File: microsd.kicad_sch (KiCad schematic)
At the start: 8 parts, among them J7 503398-1892

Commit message: bozza layout pcb
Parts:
- RN6, RN7, RN8, RN9: footprint resistor_pack_0603x4:resistor_array_0603x4 -> Resistor_SMD:R_Array_Convex_4x0603
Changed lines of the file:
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@@
+	(wire
+		(pts
+			(xy 153.67 35.56) (xy 157.48 35.56)
+		)
+		(stroke
+			(width 0)
+			(type default)
+		)
+	)
 	(wire
 		(pts
@@
 	)
 	(symbol
+		(lib_id "power:+3V3")
+		(at 153.67 35.56 90)
+		(unit 1)
+		(exclude_from_sim no)
+		(in_bom yes)
+		(on_board yes)
+		(dnp no)
+		(fields_autoplaced yes)
+		(property "Reference" "#PWR088"
+			(at 157.48 35.56 0)
+			(effects
+				(font
+					(size 1.27 1.27)
+				)
+				(hide yes)
+			)
+		)
+		(property "Value" "+3V3"
+			(at 149.86 35.5599 90)
+			(effects
+				(font
+					(size 1.27 1.27)
+				)
+				(justify left)
+			)
+		)
+		(property "Footprint" ""
+			(at 153.67 35.56 0)
+			(effects
+				(font
+					(size 1.27 1.27)
+				)
+				(hide yes)
+			)
+		)
+		(property "Datasheet" ""
+			(at 153.67 35.56 0)
+			(effects
+				(font
+					(size 1.27 1.27)
+				)
+				(hide yes)
+			)
+		)
+		(property "Description" "Power symbol creates a global label with name \"+3V3\""
+			(at 153.67 35.56 0)
+			(effects
+				(font
+					(size 1.27 1.27)
+				)
+				(hide yes)
+			)
+		)
+		(pin "1"
+		)
+		(instances
+			(project ""
+				(path "/105f6e80-8e20-4d56-8eb3-6fa826818670/5f928ec3-de2c-45ad-87ae-24994ae19594"
+					(reference "#PWR088")
+					(unit 1)
+				)
+			)
+		)
+	)
+	(symbol
 		(lib_id "Device:C_Small")
 		(at 52.07 67.31 0)
@@
 			)
 		)
-		(property "Footprint" "resistor_pack_0603x4:resistor_array_0603x4"
+		(property "Footprint" "Resistor_SMD:R_Array_Convex_4x0603"
 			(at 166.37 75.565 90)
 			(effects
@@
 			)
 		)
-		(property "Footprint" "resistor_pack_0603x4:resistor_array_0603x4"
+		(property "Footprint" "Resistor_SMD:R_Array_Convex_4x0603"
 			(at 81.915 34.29 90)
 			(effects
@@
 			)
 		)
-		(property "Footprint" "resistor_pack_0603x4:resistor_array_0603x4"
+		(property "Footprint" "Resistor_SMD:R_Array_Convex_4x0603"
 			(at 137.795 80.01 90)
 			(effects
@@
 	)
 	(symbol
+		(lib_id "power:+3.3V")
+		(at 157.48 35.56 270)
+		(unit 1)
+		(exclude_from_sim no)
+		(in_bom yes)
+		(on_board yes)
+		(dnp no)
+		(fields_autoplaced yes)
+		(property "Reference" "#PWR087"
+			(at 153.67 35.56 0)
+			(effects
+				(font
+					(size 1.27 1.27)
+				)
+				(hide yes)
+			)
+		)
+		(property "Value" "+3.3V"
+			(at 161.29 35.5599 90)
+			(effects
+				(font
+					(size 1.27 1.27)
+				)
+				(justify left)
+			)
+		)
+		(property "Footprint" ""
+			(at 157.48 35.56 0)
+			(effects
+				(font
+					(size 1.27 1.27)
+				)
+				(hide yes)
+			)
+		)
+		(property "Datasheet" ""
+			(at 157.48 35.56 0)
+			(effects
+				(font
+					(size 1.27 1.27)
+				)
+				(hide yes)
+			)
+		)
+		(property "Description" "Power symbol creates a global label with name \"+3.3V\""
+			(at 157.48 35.56 0)
+			(effects
+				(font
+					(size 1.27 1.27)
+				)
+				(hide yes)
+			)
+		)
+		(pin "1"
+		)
+		(instances
+			(project "TABv1"
+				(path "/105f6e80-8e20-4d56-8eb3-6fa826818670/5f928ec3-de2c-45ad-87ae-24994ae19594"
+					(reference "#PWR087")
+					(unit 1)
+				)
+			)
+		)
+	)
+	(symbol
 		(lib_id "Device:R_Pack04")
 		(at 45.72 48.26 90)
@@
 			)
 		)
-		(property "Footprint" "resistor_pack_0603x4:resistor_array_0603x4"
+		(property "Footprint" "Resistor_SMD:R_Array_Convex_4x0603"
 			(at 45.72 41.275 90)
 			(effects

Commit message: Corrections
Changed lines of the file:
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@@
-	(wire
-		(pts
-			(xy 153.67 35.56) (xy 157.48 35.56)
-		)
-		(stroke
-			(width 0)
-			(type default)
-		)
-	)
 	(wire
 		(pts
@@
 	)
 	(symbol
-		(lib_id "power:+3V3")
-		(at 153.67 35.56 90)
-		(unit 1)
-		(exclude_from_sim no)
-		(in_bom yes)
-		(on_board yes)
-		(dnp no)
-		(fields_autoplaced yes)
-		(property "Reference" "#PWR088"
-			(at 157.48 35.56 0)
-			(effects
-				(font
-					(size 1.27 1.27)
-				)
-				(hide yes)
-			)
-		)
-		(property "Value" "+3V3"
-			(at 149.86 35.5599 90)
-			(effects
-				(font
-					(size 1.27 1.27)
-				)
-				(justify left)
-			)
-		)
-		(property "Footprint" ""
-			(at 153.67 35.56 0)
-			(effects
-				(font
-					(size 1.27 1.27)
-				)
-				(hide yes)
-			)
-		)
-		(property "Datasheet" ""
-			(at 153.67 35.56 0)
-			(effects
-				(font
-					(size 1.27 1.27)
-				)
-				(hide yes)
-			)
-		)
-		(property "Description" "Power symbol creates a global label with name \"+3V3\""
-			(at 153.67 35.56 0)
-			(effects
-				(font
-					(size 1.27 1.27)
-				)
-				(hide yes)
-			)
-		)
-		(pin "1"
-		)
-		(instances
-			(project ""
-				(path "/105f6e80-8e20-4d56-8eb3-6fa826818670/5f928ec3-de2c-45ad-87ae-24994ae19594"
-					(reference "#PWR088")
-					(unit 1)
-				)
-			)
-		)
-	)
-	(symbol
 		(lib_id "Device:C_Small")
 		(at 52.07 67.31 0)
@@
 					(unit 1)
 				)
-			)
-		)
-	)
-	(symbol
-		(lib_id "power:+3.3V")
-		(at 157.48 35.56 270)
-		(unit 1)
-		(exclude_from_sim no)
-		(in_bom yes)
-		(on_board yes)
-		(dnp no)
-		(fields_autoplaced yes)
-		(property "Reference" "#PWR087"
-			(at 153.67 35.56 0)
-			(effects
-				(font
-					(size 1.27 1.27)
-				)
-				(hide yes)
-			)
-		)
-		(property "Value" "+3.3V"
-			(at 161.29 35.5599 90)
-			(effects
-				(font
-					(size 1.27 1.27)
-				)
-				(justify left)
-			)
-		)
-		(property "Footprint" ""
-			(at 157.48 35.56 0)
-			(effects
-				(font
-					(size 1.27 1.27)
-				)
-				(hide yes)
-			)
-		)
-		(property "Datasheet" ""
-			(at 157.48 35.56 0)
-			(effects
-				(font
-					(size 1.27 1.27)
-				)
-				(hide yes)
-			)
-		)
-		(property "Description" "Power symbol creates a global label with name \"+3.3V\""
-			(at 157.48 35.56 0)
-			(effects
-				(font
-					(size 1.27 1.27)
-				)
-				(hide yes)
-			)
-		)
-		(pin "1"
-		)
-		(instances
-			(project "TABv1"
-				(path "/105f6e80-8e20-4d56-8eb3-6fa826818670/5f928ec3-de2c-45ad-87ae-24994ae19594"
-					(reference "#PWR087")
-					(unit 1)
-				)

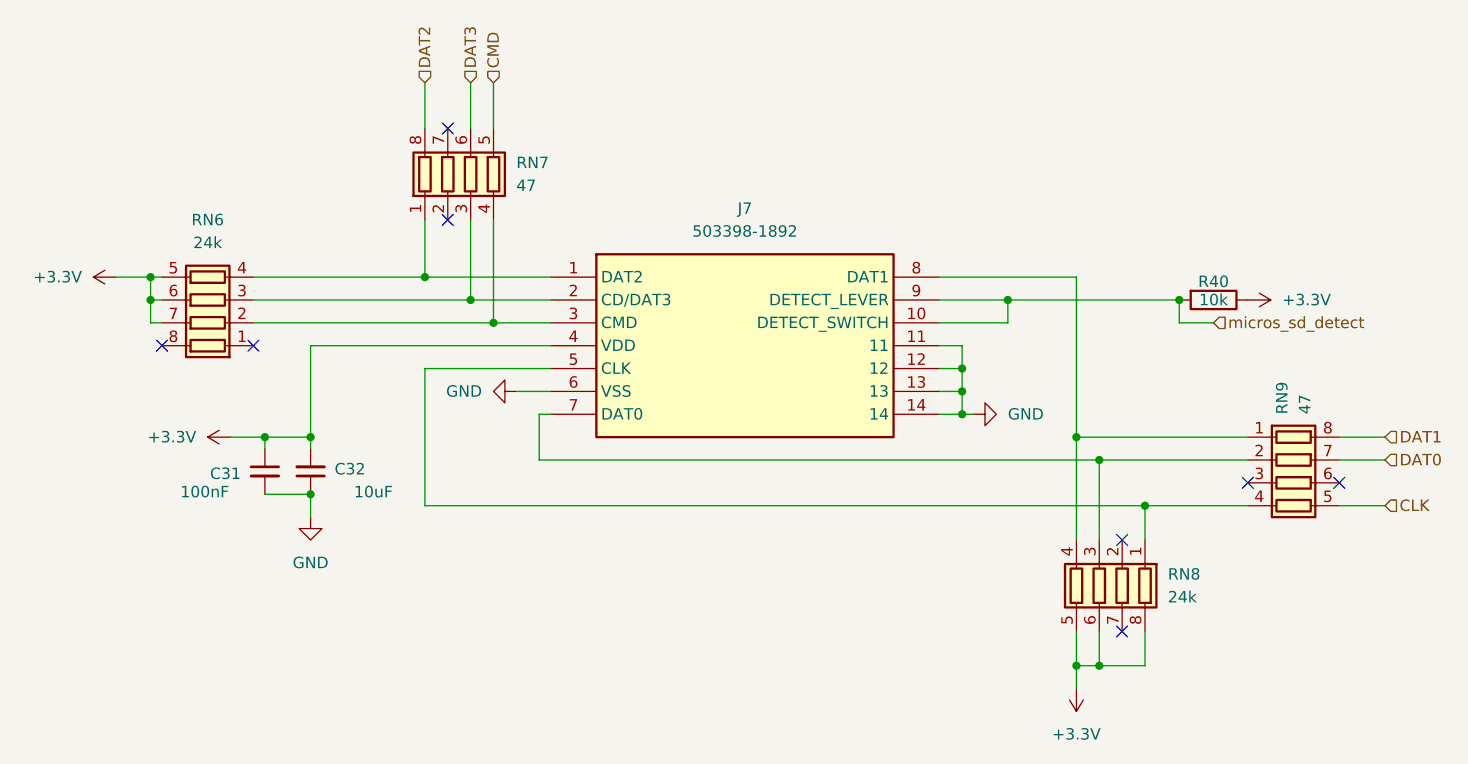
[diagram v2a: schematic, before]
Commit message: NET allignment (all on +3V3)
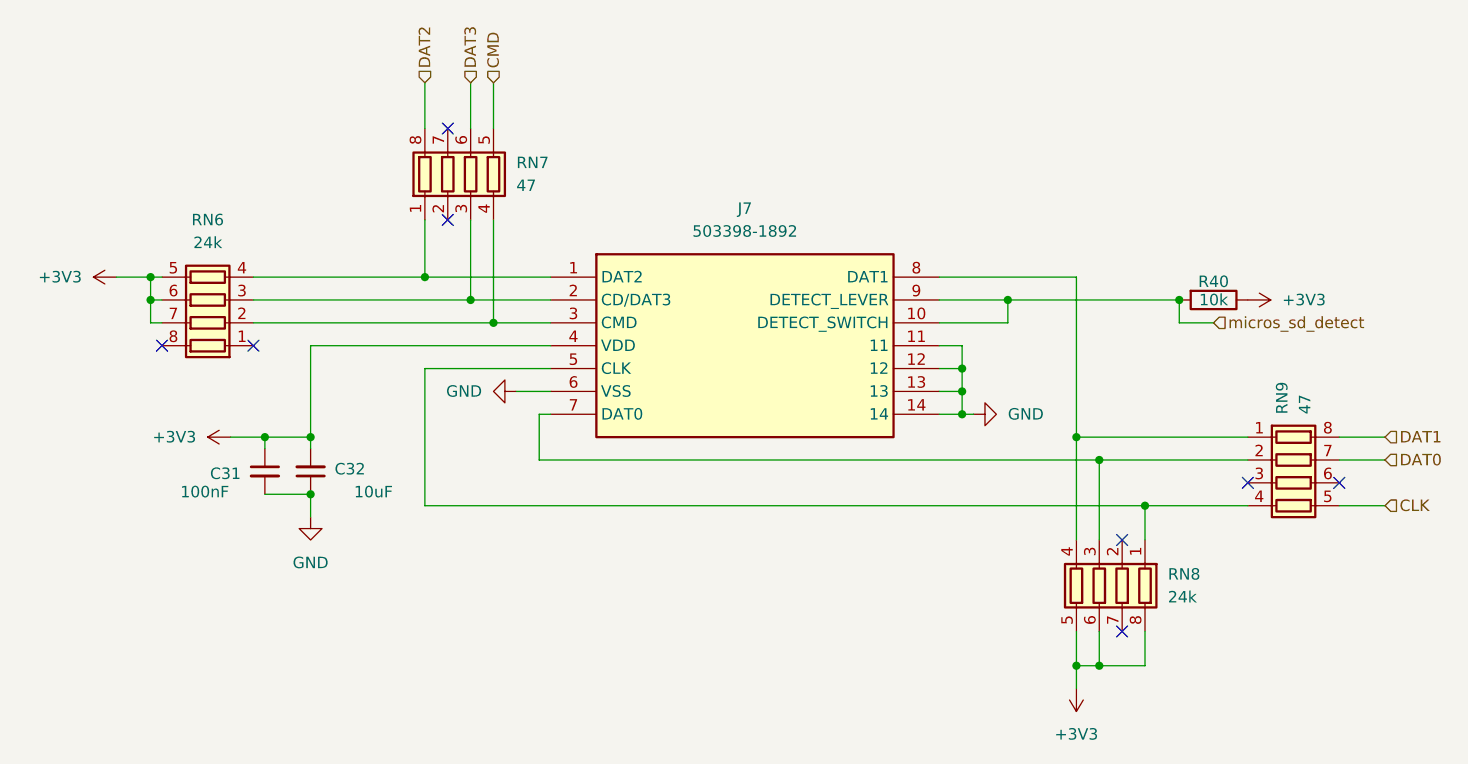
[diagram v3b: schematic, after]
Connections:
- net +3.3V renamed +3V3
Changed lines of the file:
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@@
 			)
 		)
-		(property "Value" "+3.3V"
+		(property "Value" "+3V3"
 			(at 44.45 63.4999 90)
 			(effects
@@
 			)
 		)
-		(property "Description" "Power symbol creates a global label with name \"+3.3V\""
+		(property "Description" "Power symbol creates a global label with name \"+3V3\""
 			(at 48.26 63.5 0)
 			(effects
@@
 			)
 		)
-		(property "Value" "+3.3V"
+		(property "Value" "+3V3"
 			(at 142.24 96.52 0)
 			(effects
@@
 			)
 		)
-		(property "Description" "Power symbol creates a global label with name \"+3.3V\""
+		(property "Description" "Power symbol creates a global label with name \"+3V3\""
 			(at 142.24 91.44 0)
 			(effects
@@
 			)
 		)
-		(property "Value" "+3.3V"
+		(property "Value" "+3V3"
 			(at 31.75 45.7199 90)
 			(effects
@@
 			)
 		)
-		(property "Description" "Power symbol creates a global label with name \"+3.3V\""
+		(property "Description" "Power symbol creates a global label with name \"+3V3\""
 			(at 35.56 45.72 0)
 			(effects
@@
 			)
 		)
-		(property "Value" "+3.3V"
+		(property "Value" "+3V3"
 			(at 165.1 48.2599 90)
 			(effects
@@
 			)
 		)
-		(property "Description" "Power symbol creates a global label with name \"+3.3V\""
+		(property "Description" "Power symbol creates a global label with name \"+3V3\""
 			(at 161.29 48.26 0)
 			(effects

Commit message: ROUTING
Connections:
- net CLK: now also RN9.7 (R2.2); no longer RN9.5 (R4.2)
- net DAT0: now also RN9.5 (R4.2); no longer RN9.7 (R2.2)
- net DAT2: now also J7.1 (DAT2), RN6.4 (R4.1), RN7.1 (R1.1)
- net DAT3: now also J7.2 (CD/DAT3), RN6.3 (R3.1), RN7.3 (R3.1)
- net _DAT1: now reaches J7.8 (DAT1), RN9.1 (R1.1)
- net _DAT1: now also RN8.1 (R1.1); no longer RN8.4 (R4.1)
- net at J7.7 (DAT0), RN8.3 (R3.1): now also RN9.4 (R4.1); no longer RN9.2 (R2.1)
- new net: J7.5 (CLK), RN8.4 (R4.1), RN9.2 (R2.1)
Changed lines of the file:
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@@
-	)
-	(junction
-		(at 142.24 63.5)
-		(diameter 0)
-		(color 0 0 0 0)
 	)
 	(junction
@@
 	)
 	(junction
+		(at 142.24 66.04)
+		(diameter 0)
+		(color 0 0 0 0)
+	)
+	(junction
 		(at 144.78 88.9)
 		(diameter 0)
@@
 	)
 	(junction
+		(at 144.78 71.12)
+		(diameter 0)
+		(color 0 0 0 0)
+	)
+	(junction
 		(at 129.54 60.96)
 		(diameter 0)
@@
 	)
 	(junction
-		(at 144.78 66.04)
-		(diameter 0)
-		(color 0 0 0 0)
-	)
-	(junction
 		(at 129.54 55.88)
 		(diameter 0)
@@
 	)
 	(junction
-		(at 149.86 71.12)
-		(diameter 0)
-		(color 0 0 0 0)
-	)
-	(junction
 		(at 52.07 63.5)
 		(diameter 0)
@@
 	(junction
 		(at 39.37 45.72)
+		(diameter 0)
+		(color 0 0 0 0)
+	)
+	(junction
+		(at 149.86 63.5)
 		(diameter 0)
 		(color 0 0 0 0)
@@
 	(wire
 		(pts
+			(xy 142.24 66.04) (xy 142.24 74.93)
+		)
+		(stroke
+			(width 0)
+			(type default)
+		)
+	)
+	(wire
+		(pts
 			(xy 74.93 48.26) (xy 83.82 48.26)
 		)
@@
 	(wire
 		(pts
-			(xy 149.86 71.12) (xy 161.29 71.12)
-		)
-		(stroke
-			(width 0)
-			(type default)
-		)
-	)
-	(wire
-		(pts
 			(xy 77.47 24.13) (xy 77.47 29.21)
 		)
@@
 	(wire
 		(pts
-			(xy 142.24 63.5) (xy 142.24 74.93)
-		)
-		(stroke
-			(width 0)
-			(type default)
-		)
-	)
-	(wire
-		(pts
 			(xy 129.54 53.34) (xy 129.54 55.88)
 		)
@@
 	(wire
 		(pts
+			(xy 142.24 45.72) (xy 142.24 63.5)
+		)
+		(stroke
+			(width 0)
+			(type default)
+		)
+	)
+	(wire
+		(pts
 			(xy 134.62 48.26) (xy 153.67 48.26)
 		)
@@
 	(wire
 		(pts
-			(xy 82.55 66.04) (xy 144.78 66.04)
+			(xy 82.55 71.12) (xy 144.78 71.12)
 		)
 		(stroke
@@
 	(wire
 		(pts
-			(xy 142.24 63.5) (xy 161.29 63.5)
+			(xy 142.24 63.5) (xy 149.86 63.5)
 		)
 		(stroke
@@
 	(wire
 		(pts
-			(xy 144.78 66.04) (xy 161.29 66.04)
-		)
-		(stroke
-			(width 0)
-			(type default)
-		)
-	)
-	(wire
-		(pts
-			(xy 69.85 55.88) (xy 69.85 71.12)
+			(xy 142.24 66.04) (xy 161.29 66.04)
+		)
+		(stroke
+			(width 0)
+			(type default)
+		)
+	)
+	(wire
+		(pts
+			(xy 69.85 55.88) (xy 69.85 66.04)
 		)
 		(stroke
@@
 	(wire
 		(pts
-			(xy 142.24 45.72) (xy 142.24 63.5)
-		)
-		(stroke
-			(width 0)
-			(type default)
-		)
-	)
-	(wire
-		(pts
 			(xy 39.37 48.26) (xy 39.37 50.8)
 		)
@@
 	(wire
 		(pts
-			(xy 69.85 71.12) (xy 149.86 71.12)
+			(xy 69.85 66.04) (xy 142.24 66.04)
 		)
 		(stroke
@@
 	(wire
 		(pts
+			(xy 144.78 71.12) (xy 161.29 71.12)
+		)
+		(stroke
+			(width 0)
+			(type default)
+		)
+	)
+	(wire
+		(pts
 			(xy 127 55.88) (xy 129.54 55.88)
 		)
@@
 	(wire
 		(pts
-			(xy 82.55 60.96) (xy 82.55 66.04)
+			(xy 82.55 60.96) (xy 82.55 71.12)
 		)
 		(stroke
@@
 	(wire
 		(pts
-			(xy 144.78 66.04) (xy 144.78 74.93)
-		)
-		(stroke
-			(width 0)
-			(type default)
-		)
-	)
-	(wire
-		(pts
-			(xy 149.86 71.12) (xy 149.86 74.93)
+			(xy 149.86 63.5) (xy 149.86 74.93)
 		)
 		(stroke
@@
 	(wire
 		(pts
+			(xy 144.78 71.12) (xy 144.78 74.93)
+		)
+		(stroke
+			(width 0)
+			(type default)
+		)
+	)
+	(wire
+		(pts
 			(xy 74.93 39.37) (xy 74.93 48.26)
 		)
@@
 	(wire
 		(pts
+			(xy 149.86 63.5) (xy 161.29 63.5)
+		)
+		(stroke
+			(width 0)
+			(type default)
+		)
+	)
+	(wire
+		(pts
 			(xy 57.15 63.5) (xy 57.15 64.77)
 		)
@@
 		)
 	)
-	(hierarchical_label "DAT0"
+	(label "DAT3"
+		(at 78.74 48.26 0)
+		(effects
+			(font
+				(size 1.27 1.27)
+			)
+			(justify left bottom)
+		)
+	)
+	(label "DAT2"
+		(at 78.74 45.72 0)
+		(effects
+			(font
+				(size 1.27 1.27)
+			)
+			(justify left bottom)
+		)
+	)
+	(label "_DAT1"
+		(at 132.08 45.72 0)
+		(effects
+			(font
+				(size 1.27 1.27)
+			)
+			(justify left bottom)
+		)
+	)
+	(hierarchical_label "CLK"
 		(shape input)
 		(at 176.53 66.04 0)
@@
 		)
 	)
+	(hierarchical_label "DAT0"
+		(shape input)
+		(at 176.53 71.12 0)
+		(effects
+			(font
+				(size 1.27 1.27)
+			)
+			(justify left)
+		)
+	)
 	(hierarchical_label "DAT3"
 		(shape input)
@@
 		(effects
 			(font
-				(size 1.27 1.27)
-			)
-			(justify left)
-		)
-	)
-	(hierarchical_label "CLK"
-		(shape input)
-		(at 176.53 71.12 0)
-		(effects
-			(font

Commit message: Routing 06/25
Molte modifiche
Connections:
- net +3V3: now also RN6.8 (R1.2); no longer RN6.7 (R2.2)
- net CMD: now also RN7.6 (R3.2); no longer RN7.5 (R4.2)
- net DAT2: now also RN7.5 (R4.2); no longer J7.1 (DAT2), RN6.4 (R4.1), RN7.1 (R1.1), RN7.8 (R1.2)
- net DAT3: now also RN7.8 (R1.2); no longer J7.2 (CD/DAT3), RN6.3 (R3.1), RN7.3 (R3.1), RN7.6 (R3.2)
- net at RN6.1 (R1.1): now also J7.3 (CMD), RN7.3 (R3.1)
- new net _DAT2: J7.1 (DAT2), RN6.4 (R4.1), RN7.4 (R4.1)
- new net _DAT3: J7.2 (CD/DAT3), RN6.3 (R3.1), RN7.1 (R1.1)
- now unconnected: RN6.2 (R2.1)
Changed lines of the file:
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@@
-	)
-	(junction
-		(at 74.93 48.26)
-		(diameter 0)
-		(color 0 0 0 0)
 	)
 	(junction
@@
 	)
 	(junction
+		(at 74.93 50.8)
+		(diameter 0)
+		(color 0 0 0 0)
+	)
+	(junction
+		(at 144.78 71.12)
+		(diameter 0)
+		(color 0 0 0 0)
+	)
+	(junction
+		(at 129.54 60.96)
+		(diameter 0)
+		(color 0 0 0 0)
+	)
+	(junction
+		(at 129.54 55.88)
+		(diameter 0)
+		(color 0 0 0 0)
+	)
+	(junction
+		(at 69.85 48.26)
+		(diameter 0)
+		(color 0 0 0 0)
+	)
+	(junction
+		(at 57.15 69.85)
+		(diameter 0)
+		(color 0 0 0 0)
+	)
+	(junction
+		(at 52.07 63.5)
+		(diameter 0)
+		(color 0 0 0 0)
+	)
+	(junction
 		(at 39.37 48.26)
 		(diameter 0)
@@
 	)
 	(junction
-		(at 144.78 71.12)
-		(diameter 0)
-		(color 0 0 0 0)
-	)
-	(junction
-		(at 129.54 60.96)
-		(diameter 0)
-		(color 0 0 0 0)
-	)
-	(junction
-		(at 69.85 45.72)
-		(diameter 0)
-		(color 0 0 0 0)
-	)
-	(junction
-		(at 129.54 55.88)
-		(diameter 0)
-		(color 0 0 0 0)
-	)
-	(junction
-		(at 57.15 69.85)
-		(diameter 0)
-		(color 0 0 0 0)
-	)
-	(junction
-		(at 52.07 63.5)
-		(diameter 0)
-		(color 0 0 0 0)
-	)
-	(junction
 		(at 39.37 45.72)
 		(diameter 0)
@@
 	)
 	(junction
-		(at 77.47 50.8)
+		(at 77.47 45.72)
 		(diameter 0)
 		(color 0 0 0 0)
@@
 	)
 	(no_connect
+		(at 40.64 50.8)
+	)
+	(no_connect
 		(at 147.32 85.09)
-	)
-	(no_connect
-		(at 50.8 53.34)
 	)
 	(no_connect
@@
 	)
 	(no_connect
+		(at 50.8 50.8)
+	)
+	(no_connect
 		(at 171.45 68.58)
-	)
-	(no_connect
-		(at 40.64 53.34)
 	)
 	(no_connect
@@
 	(wire
 		(pts
-			(xy 74.93 48.26) (xy 83.82 48.26)
-		)
-		(stroke
-			(width 0)
-			(type default)
-		)
-	)
-	(wire
-		(pts
 			(xy 129.54 60.96) (xy 130.81 60.96)
 		)
@@
 	(wire
 		(pts
+			(xy 53.34 50.8) (xy 53.34 53.34)
+		)
+		(stroke
+			(width 0)
+			(type default)
+		)
+	)
+	(wire
+		(pts
 			(xy 52.07 63.5) (xy 57.15 63.5)
 		)
@@
 	(wire
 		(pts
+			(xy 69.85 48.26) (xy 83.82 48.26)
+		)
+		(stroke
+			(width 0)
+			(type default)
+		)
+	)
+	(wire
+		(pts
 			(xy 83.82 55.88) (xy 69.85 55.88)
 		)
@@
 	(wire
 		(pts
+			(xy 74.93 39.37) (xy 74.93 50.8)
+		)
+		(stroke
+			(width 0)
+			(type default)
+		)
+	)
+	(wire
+		(pts
 			(xy 48.26 63.5) (xy 52.07 63.5)
 		)
@@
 	(wire
 		(pts
-			(xy 77.47 50.8) (xy 83.82 50.8)
+			(xy 50.8 45.72) (xy 77.47 45.72)
 		)
 		(stroke
@@
 	(wire
 		(pts
+			(xy 40.64 53.34) (xy 39.37 53.34)
+		)
+		(stroke
+			(width 0)
+			(type default)
+		)
+	)
+	(wire
+		(pts
+			(xy 74.93 50.8) (xy 83.82 50.8)
+		)
+		(stroke
+			(width 0)
+			(type default)
+		)
+	)
+	(wire
+		(pts
 			(xy 142.24 45.72) (xy 142.24 63.5)
 		)
@@
 	(wire
 		(pts
-			(xy 69.85 39.37) (xy 69.85 45.72)
-		)
-		(stroke
-			(width 0)
-			(type default)
-		)
-	)
-	(wire
-		(pts
 			(xy 83.82 60.96) (xy 82.55 60.96)
 		)
@@
 	(wire
 		(pts
+			(xy 77.47 45.72) (xy 83.82 45.72)
+		)
+		(stroke
+			(width 0)
+			(type default)
+		)
+	)
+	(wire
+		(pts
 			(xy 35.56 45.72) (xy 39.37 45.72)
 		)
@@
 	(wire
 		(pts
-			(xy 50.8 50.8) (xy 77.47 50.8)
+			(xy 77.47 39.37) (xy 77.47 45.72)
 		)
 		(stroke
@@
 	(wire
 		(pts
-			(xy 50.8 48.26) (xy 74.93 48.26)
+			(xy 50.8 48.26) (xy 69.85 48.26)
 		)
 		(stroke
@@
 	(wire
 		(pts
-			(xy 39.37 48.26) (xy 39.37 50.8)
-		)
-		(stroke
-			(width 0)
-			(type default)
-		)
-	)
-	(wire
-		(pts
 			(xy 144.78 88.9) (xy 149.86 88.9)
 		)
@@
 	(wire
 		(pts
-			(xy 77.47 39.37) (xy 77.47 50.8)
-		)
-		(stroke
-			(width 0)
-			(type default)
-		)
-	)
-	(wire
-		(pts
 			(xy 57.15 53.34) (xy 83.82 53.34)
 		)
@@
 	(wire
 		(pts
-			(xy 39.37 50.8) (xy 40.64 50.8)
+			(xy 53.34 50.8) (xy 74.93 50.8)
 		)
 		(stroke
@@
 	(wire
 		(pts
-			(xy 69.85 45.72) (xy 83.82 45.72)
-		)
-		(stroke
-			(width 0)
-			(type default)
-		)
-	)
-	(wire
-		(pts
 			(xy 171.45 63.5) (xy 176.53 63.5)
 		)
@@
 	(wire
 		(pts
-			(xy 50.8 45.72) (xy 69.85 45.72)
+			(xy 53.34 53.34) (xy 50.8 53.34)
 		)
 		(stroke
@@
 	(wire
 		(pts
+			(xy 69.85 39.37) (xy 69.85 48.26)
+		)
+		(stroke
+			(width 0)
+			(type default)
+		)
+	)
+	(wire
+		(pts
 			(xy 153.67 48.26) (xy 153.67 50.8)
 		)
@@
 	(wire
 		(pts
-			(xy 74.93 39.37) (xy 74.93 48.26)
-		)
-		(stroke
-			(width 0)
-			(type default)
-		)
-	)
-	(wire
-		(pts
 			(xy 149.86 63.5) (xy 161.29 63.5)
 		)
@@
 	(wire
 		(pts
+			(xy 39.37 53.34) (xy 39.37 48.26)
+		)
+		(stroke
+			(width 0)
+			(type default)
+		)
+	)
+	(wire
+		(pts
 			(xy 57.15 63.5) (xy 57.15 64.77)
 		)
@@
 		)
 	)
-	(label "DAT3"
+	(label "_DAT3"
 		(at 78.74 48.26 0)
 		(effects
@@
 		)
 	)
-	(label "DAT2"
+	(label "_DAT2"
 		(at 78.74 45.72 0)
 		(effects
@@
 			)
 			(justify left bottom)
+		)
+	)
+	(hierarchical_label "DAT3"
+		(shape input)
+		(at 69.85 24.13 90)
+		(effects
+			(font
+				(size 1.27 1.27)
+			)
+			(justify left)
 		)
 	)
@@
 	(hierarchical_label "DAT2"
 		(shape input)
-		(at 69.85 24.13 90)
+		(at 77.47 24.13 90)
+		(effects
+			(font
+				(size 1.27 1.27)
+			)
+			(justify left)
+		)
+	)
+	(hierarchical_label "CMD"
+		(shape input)
+		(at 74.93 24.13 90)
 		(effects
 			(font
@@
 		)
 	)
-	(hierarchical_label "DAT3"
-		(shape input)
-		(at 74.93 24.13 90)
-		(effects
-			(font
-				(size 1.27 1.27)
-			)
-			(justify left)
-		)
-	)
 	(hierarchical_label "DAT1"
 		(shape input)
@@
 		(effects
 			(font
-				(size 1.27 1.27)
-			)
-			(justify left)
-		)
-	)
-	(hierarchical_label "CMD"
-		(shape input)
-		(at 77.47 24.13 90)
-		(effects
-			(font

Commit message: Names fix
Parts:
- C32: value 10uF -> 10uf
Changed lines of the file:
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@@
 			)
 		)
-		(property "Value" "10uF"
+		(property "Value" "10uf"
 			(at 66.294 69.596 0)
 			(effects
